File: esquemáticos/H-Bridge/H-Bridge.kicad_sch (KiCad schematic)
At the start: 5 parts, among them M1 DC_Motor_h, Q1 IRF510, Q2 IRF9540N, Q3 IRF9540N, Q4 IRF510

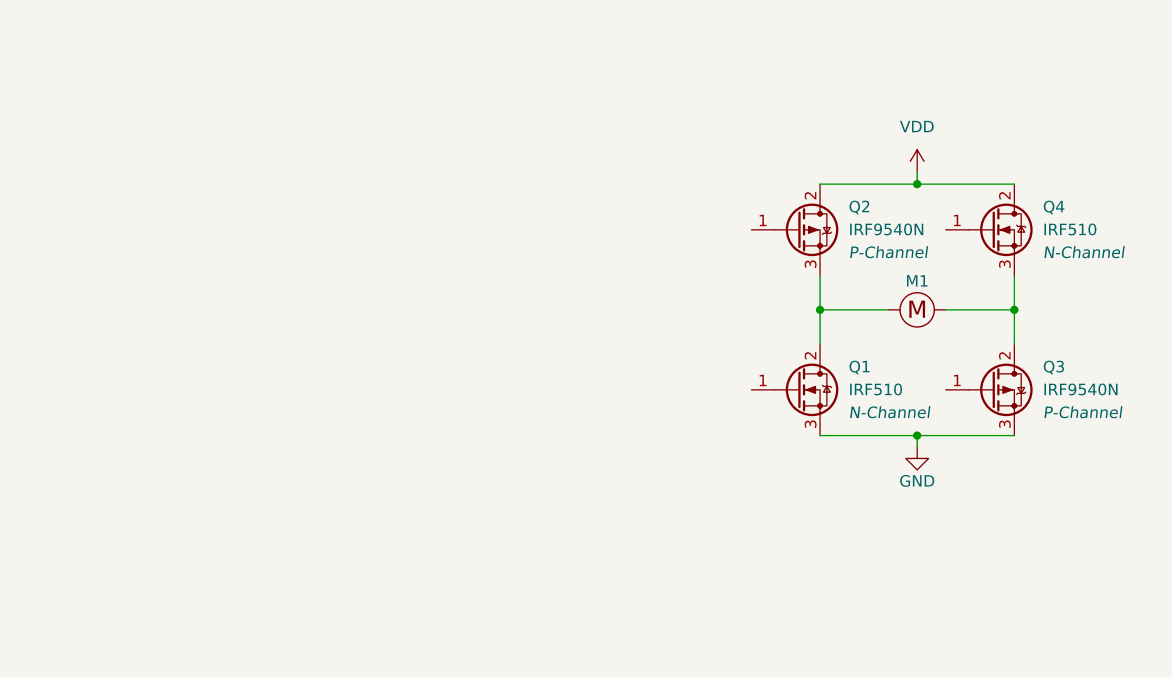
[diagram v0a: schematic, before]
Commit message: Puente H actualizado
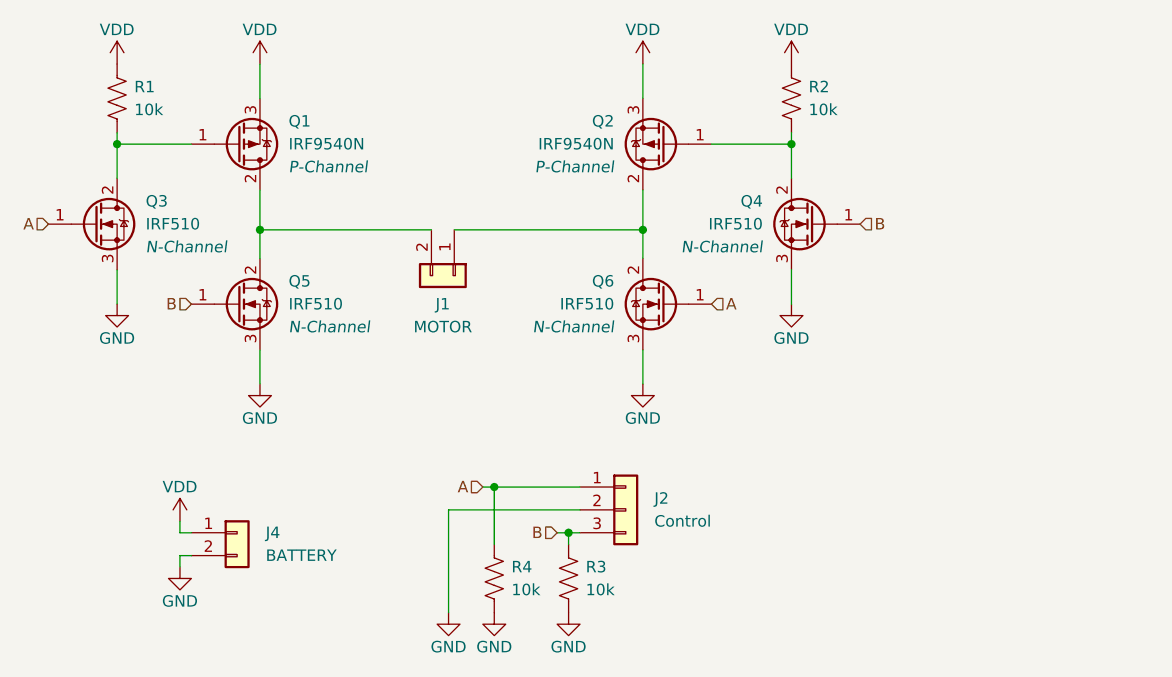
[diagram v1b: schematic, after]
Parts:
- removed M1: DC_Motor_h, symbol generic:DC_Motor_h
- removed Q3: IRF9540N, Package_TO_SOT_THT:TO-220-3_Vertical, symbol Transistor_FET:IRF9540N
- added J1: MOTOR, TerminalBlock:TerminalBlock_Altech_AK300-2_P5.00mm, symbol Connector_Generic:Conn_01x02
- added J2: Control, Connector_PinHeader_2.54mm:PinHeader_1x03_P2.54mm_Vertical, symbol Connector_Generic:Conn_01x03
- added J4: BATTERY, TerminalBlock:TerminalBlock_Altech_AK300-2_P5.00mm, symbol Connector_Generic:Conn_01x02
- added Q2: IRF9540N, Package_TO_SOT_THT:TO-220-3_Horizontal_TabDown, symbol Transistor_FET:IRF9540N
- added Q3, Q6: IRF510, Package_TO_SOT_THT:TO-220-3_Horizontal_TabDown, symbol Transistor_FET:IRF540N
- added R1, R2, R3, R4: 10k, Resistor_THT:R_Axial_DIN0309_L9.0mm_D3.2mm_P12.70mm_Horizontal, symbol Device:R_US
- Q1: renamed from Q2; footprint Package_TO_SOT_THT:TO-220-3_Vertical -> Package_TO_SOT_THT:TO-220-3_Horizontal_TabDown
- Q4: footprint Package_TO_SOT_THT:TO-220-3_Vertical -> Package_TO_SOT_THT:TO-220-3_Horizontal_TabDown
- Q5: renamed from Q1; footprint Package_TO_SOT_THT:TO-220-3_Vertical -> Package_TO_SOT_THT:TO-220-3_Horizontal_TabDown
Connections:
- net GND: now also Q4.3 (S), J2.2 (Pin_2), J4.2 (Pin_2), Q3.3 (S), Q6.3 (S), R3.2, R4.2
- net VDD: now also Q1.3 (S), J4.1 (Pin_1), Q2.3 (S), R1.1, R2.1; no longer Q1.2 (D), Q4.2 (D)
- net at Q1.1 (G): now also Q3.2 (D), R1.2
- net at Q5.2 (D): now also Q1.2 (D), J1.2 (Pin_2); no longer Q1.3 (S)
- net B: now reaches Q5.1 (G)
- net B: now also Q4.1 (G), J2.3 (Pin_3), R3.1
- new net: J1.1 (Pin_1), Q2.2 (D), Q6.2 (D)
- new net: Q2.1 (G), Q4.2 (D), R2.2
- new net A: J2.1 (Pin_1), Q3.1 (G), Q6.1 (G), R4.1
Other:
- company: (none) -> Grupo 33 - Sistemas Electrónicos Digitales
- title: (none) -> Puente H
- moved on the sheet: Q1, Q5

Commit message: Esquemáticos completos
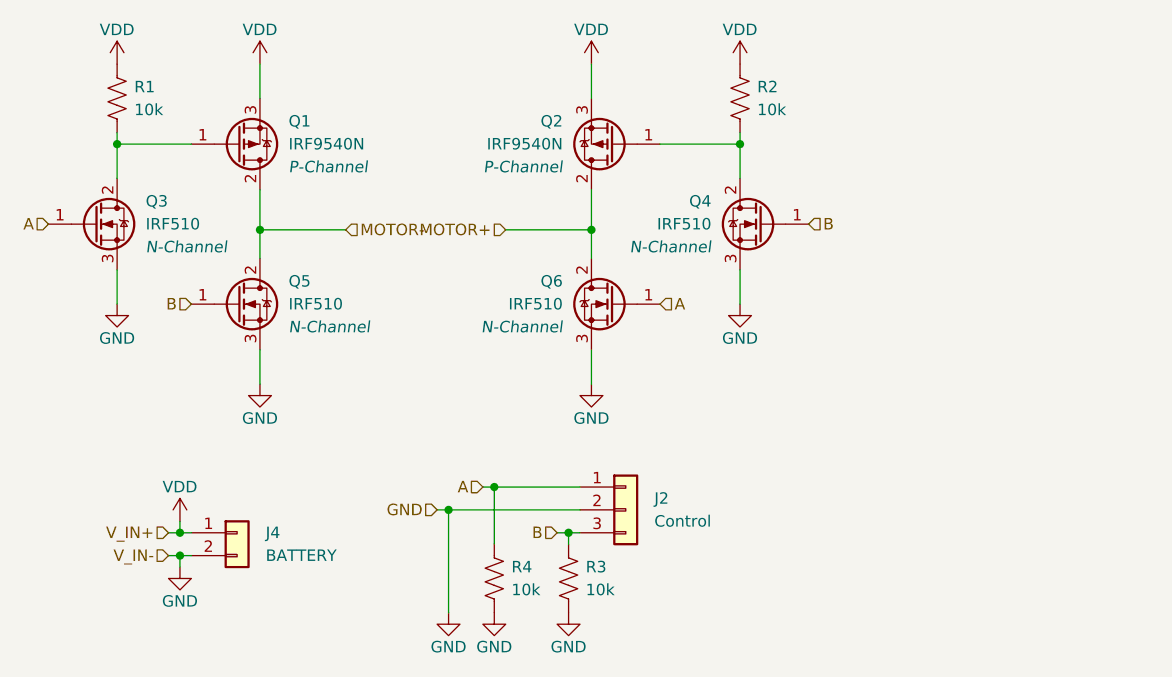
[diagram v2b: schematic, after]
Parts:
- removed J1: MOTOR, TerminalBlock:TerminalBlock_Altech_AK300-2_P5.00mm, symbol Connector_Generic:Conn_01x02
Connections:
- net MOTOR+: now reaches Q2.2 (D), Q6.2 (D)
- net MOTOR-: now reaches Q1.2 (D), Q5.2 (D)
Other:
- moved on the sheet: Q2, Q4, Q6, R2
